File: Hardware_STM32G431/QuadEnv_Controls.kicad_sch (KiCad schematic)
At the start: 14 parts, among them J1 Conn_01x04_Male, J2 Conn_01x05_Male, J3 Conn_01x04_Male, J4 Conn_01x04_Male, J5 Gate_Out, J6 Env_Out

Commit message: First draft of Panel complete
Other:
- company: (none) -> Mountjoy Modular
- title: (none) -> QuadEnv Controls
- moved on the sheet: D1, D2, D3, D4, J4, J5, J6, RV1, RV2, RV3, RV4

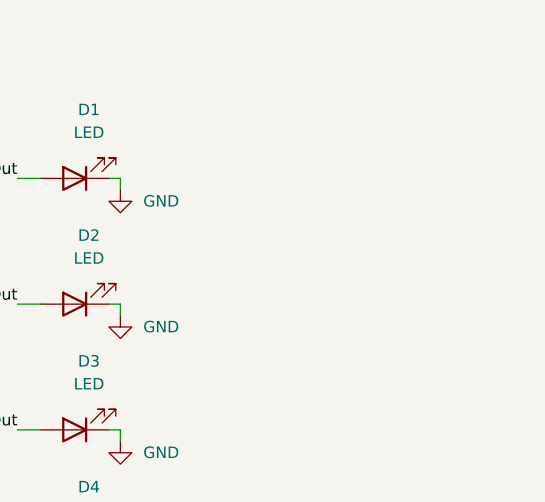
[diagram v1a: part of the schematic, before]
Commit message: Added PWM Test code
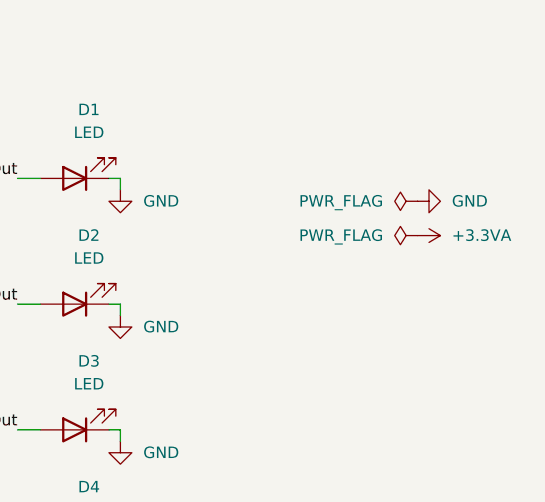
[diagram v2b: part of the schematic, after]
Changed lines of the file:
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@@
     (pin "4")
+  )
+  (symbol (lib_id "power:PWR_FLAG") (at 241.3 46.99 90) (unit 1)
+    (in_bom yes) (on_board yes) (fields_autoplaced)
+    (property "Reference" "#FLG02" (id 0) (at 239.395 46.99 0)
+      (effects (font (size 1.27 1.27)) hide)
+    )
+    (property "Value" "PWR_FLAG" (id 1) (at 237.49 46.9899 90)
+      (effects (font (size 1.27 1.27)) (justify left))
+    )
+    (property "Footprint" "" (id 2) (at 241.3 46.99 0)
+      (effects (font (size 1.27 1.27)) hide)
+    )
+    (property "Datasheet" "~" (id 3) (at 241.3 46.99 0)
+      (effects (font (size 1.27 1.27)) hide)
+    )
+    (pin "1")
   )
   (symbol (lib_id "Device:LED") (at 203.2 40.64 180) (unit 1)
@@
     (pin "2")
   )
+  (symbol (lib_id "power:PWR_FLAG") (at 241.3 43.18 90) (unit 1)
+    (in_bom yes) (on_board yes) (fields_autoplaced)
+    (property "Reference" "#FLG01" (id 0) (at 239.395 43.18 0)
+      (effects (font (size 1.27 1.27)) hide)
+    )
+    (property "Value" "PWR_FLAG" (id 1) (at 237.49 43.1799 90)
+      (effects (font (size 1.27 1.27)) (justify left))
+    )
+    (property "Footprint" "" (id 2) (at 241.3 43.18 0)
+      (effects (font (size 1.27 1.27)) hide)
+    )
+    (property "Datasheet" "~" (id 3) (at 241.3 43.18 0)
+      (effects (font (size 1.27 1.27)) hide)
+    )
+    (pin "1")
+  )
   (symbol (lib_id "Connector:Conn_01x05_Male") (at 59.69 44.45 0) (unit 1)
     (in_bom yes) (on_board yes)
@@
     (pin "4")
   )
+  (symbol (lib_id "power:GND") (at 241.3 43.18 90) (mirror x) (unit 1)
+    (in_bom yes) (on_board yes) (fields_autoplaced)
+    (property "Reference" "#PWR01" (id 0) (at 247.65 43.18 0)
+      (effects (font (size 1.27 1.27)) hide)
+    )
+    (property "Value" "GND" (id 1) (at 245.11 43.1799 90)
+      (effects (font (size 1.27 1.27)) (justify right))
+    )
+    (property "Footprint" "" (id 2) (at 241.3 43.18 0)
+      (effects (font (size 1.27 1.27)) hide)
+    )
+    (property "Datasheet" "" (id 3) (at 241.3 43.18 0)
+      (effects (font (size 1.27 1.27)) hide)
+    )
+    (pin "1")
+  )
   (symbol (lib_id "Device:R_Potentiometer") (at 106.68 49.53 0) (unit 1)
     (in_bom yes) (on_board yes) (fields_autoplaced)
@@
     (pin "2")
     (pin "3")
+  )
+  (symbol (lib_id "power:+3.3VA") (at 241.3 46.99 270) (unit 1)
+    (in_bom yes) (on_board yes) (fields_autoplaced)
+    (property "Reference" "#PWR02" (id 0) (at 237.49 46.99 0)
+      (effects (font (size 1.27 1.27)) hide)
+    )
+    (property "Value" "+3.3VA" (id 1) (at 245.11 46.9899 90)
+      (effects (font (size 1.27 1.27)) (justify left))
+    )
+    (property "Footprint" "" (id 2) (at 241.3 46.99 0)
+      (effects (font (size 1.27 1.27)) hide)
+    )
+    (property "Datasheet" "" (id 3) (at 241.3 46.99 0)
+      (effects (font (size 1.27 1.27)) hide)
+    )
+    (pin "1")
   )
   (symbol (lib_id "Device:LED") (at 203.2 68.58 180) (unit 1)
@@
   )
   (symbol_instances
+    (path "/781d2827-8c57-4c8c-a90e-7fa9a8e3bce3"
+      (reference "#FLG01") (unit 1) (value "PWR_FLAG") (footprint "")
+    )
+    (path "/14afa5e3-66d5-4d5e-b805-932a5af80e37"
+      (reference "#FLG02") (unit 1) (value "PWR_FLAG") (footprint "")
+    )
+    (path "/8b2a71f8-8e19-4c07-809c-0b6873192b65"
+      (reference "#PWR01") (unit 1) (value "GND") (footprint "")
+    )
+    (path "/a579e8f5-f380-4350-a981-d76dba1a11f6"
+      (reference "#PWR02") (unit 1) (value "+3.3VA") (footprint "")
+    )
     (path "/b39f733d-e3d6-4862-b7be-1e5e202f5a4b"
       (reference "#PWR05") (unit 1) (value "+3.3VA") (footprint "")

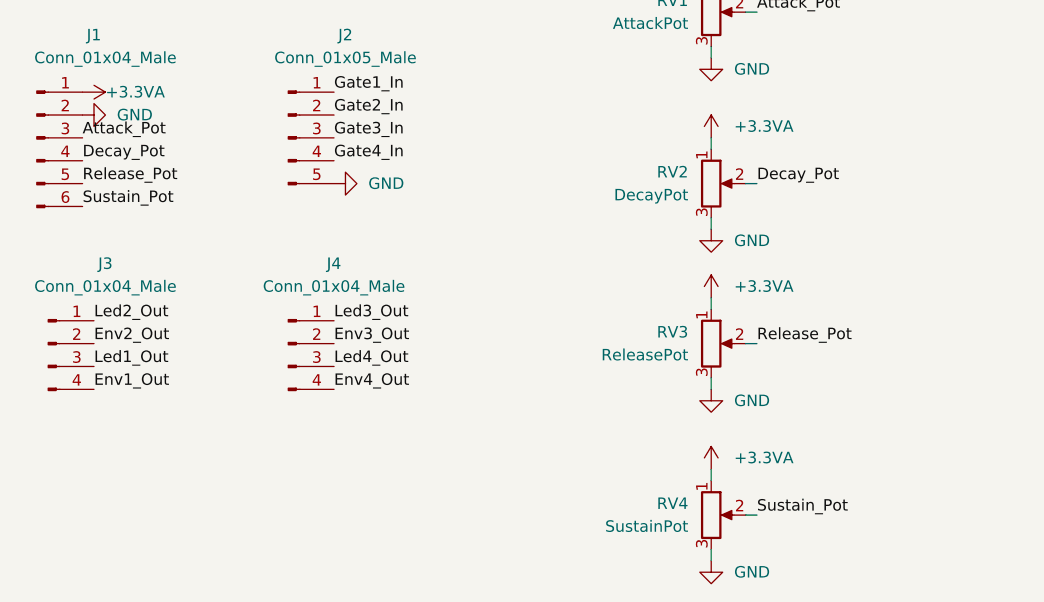
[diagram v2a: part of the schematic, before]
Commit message: Corrections to schematic to fix sustain and release pots being switched
+Updated project to use production module parts and connections
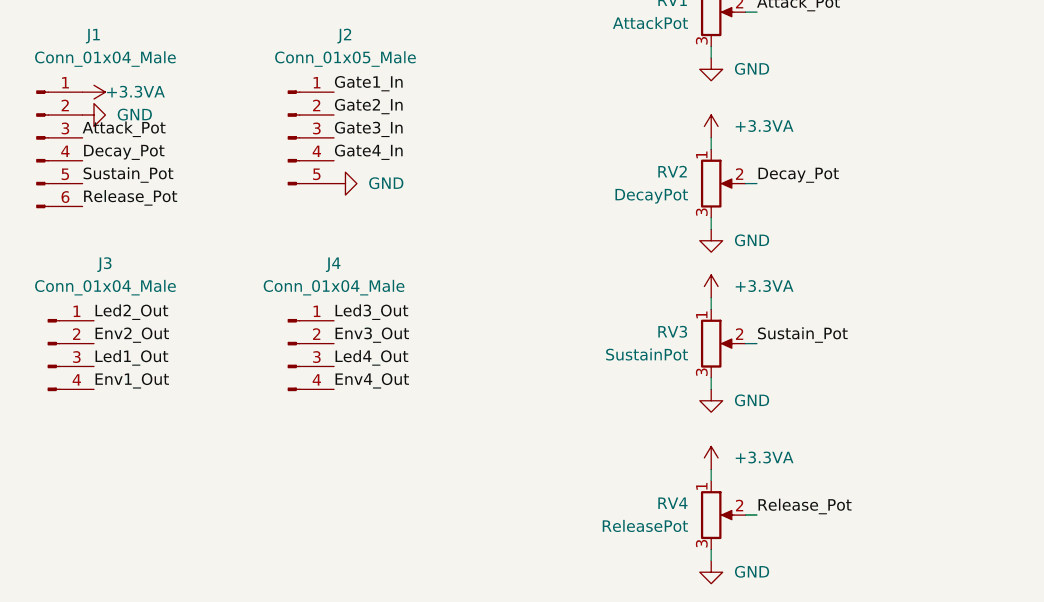
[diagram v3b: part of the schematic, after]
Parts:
- RV3: value ReleasePot -> SustainPot
- RV4: value SustainPot -> ReleasePot
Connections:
- net Release_Pot: now also J1.6 (Pin_6), RV4.2; no longer J1.5 (Pin_5), RV3.2
- net Sustain_Pot: now also J1.5 (Pin_5), RV3.2; no longer J1.6 (Pin_6), RV4.2
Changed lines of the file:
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@@
     (effects (font (size 1.27 1.27)) (justify right bottom))
   )
-  (label "Sustain_Pot" (at 36.83 52.07 0)
+  (label "Sustain_Pot" (at 36.83 49.53 0)
     (effects (font (size 1.27 1.27)) (justify left bottom))
   )
@@
     (effects (font (size 1.27 1.27)) (justify left bottom))
   )
-  (label "Release_Pot" (at 111.76 67.31 0)
+  (label "Release_Pot" (at 111.76 86.36 0)
     (effects (font (size 1.27 1.27)) (justify left bottom))
   )
@@
     (effects (font (size 1.27 1.27)) (justify left bottom))
   )
-  (label "Release_Pot" (at 36.83 49.53 0)
+  (label "Release_Pot" (at 36.83 52.07 0)
     (effects (font (size 1.27 1.27)) (justify left bottom))
   )
@@
     (effects (font (size 1.27 1.27)) (justify left bottom))
   )
-  (label "Sustain_Pot" (at 111.76 86.36 0)
+  (label "Sustain_Pot" (at 111.76 67.31 0)
     (effects (font (size 1.27 1.27)) (justify left bottom))
   )
@@
       (effects (font (size 1.27 1.27)) (justify right))
     )
-    (property "Value" "SustainPot" (id 1) (at 104.14 87.6299 0)
+    (property "Value" "ReleasePot" (id 1) (at 104.14 87.6299 0)
       (effects (font (size 1.27 1.27)) (justify right))
     )
@@
       (effects (font (size 1.27 1.27)) (justify right))
     )
-    (property "Value" "ReleasePot" (id 1) (at 104.14 68.5799 0)
+    (property "Value" "SustainPot" (id 1) (at 104.14 68.5799 0)
       (effects (font (size 1.27 1.27)) (justify right))
     )
@@
     )
     (path "/3fb71fd2-1e6c-4fed-be40-5f5a7bfb3908"
-      (reference "RV3") (unit 1) (value "ReleasePot") (footprint "Custom_Footprints:Alpha_9mm_Potentiometer_Aligned")
+      (reference "RV3") (unit 1) (value "SustainPot") (footprint "Custom_Footprints:Alpha_9mm_Potentiometer_Aligned")
     )
     (path "/191ea6f3-0ad2-4f71-8573-7510f6af6ffa"
-      (reference "RV4") (unit 1) (value "SustainPot") (footprint "Custom_Footprints:Alpha_9mm_Potentiometer_Aligned")
-    )
-  )
+      (reference "RV4") (unit 1) (value "ReleasePot") (footprint "Custom_Footprints:Alpha_9mm_Potentiometer_Aligned")
+    )
+  )

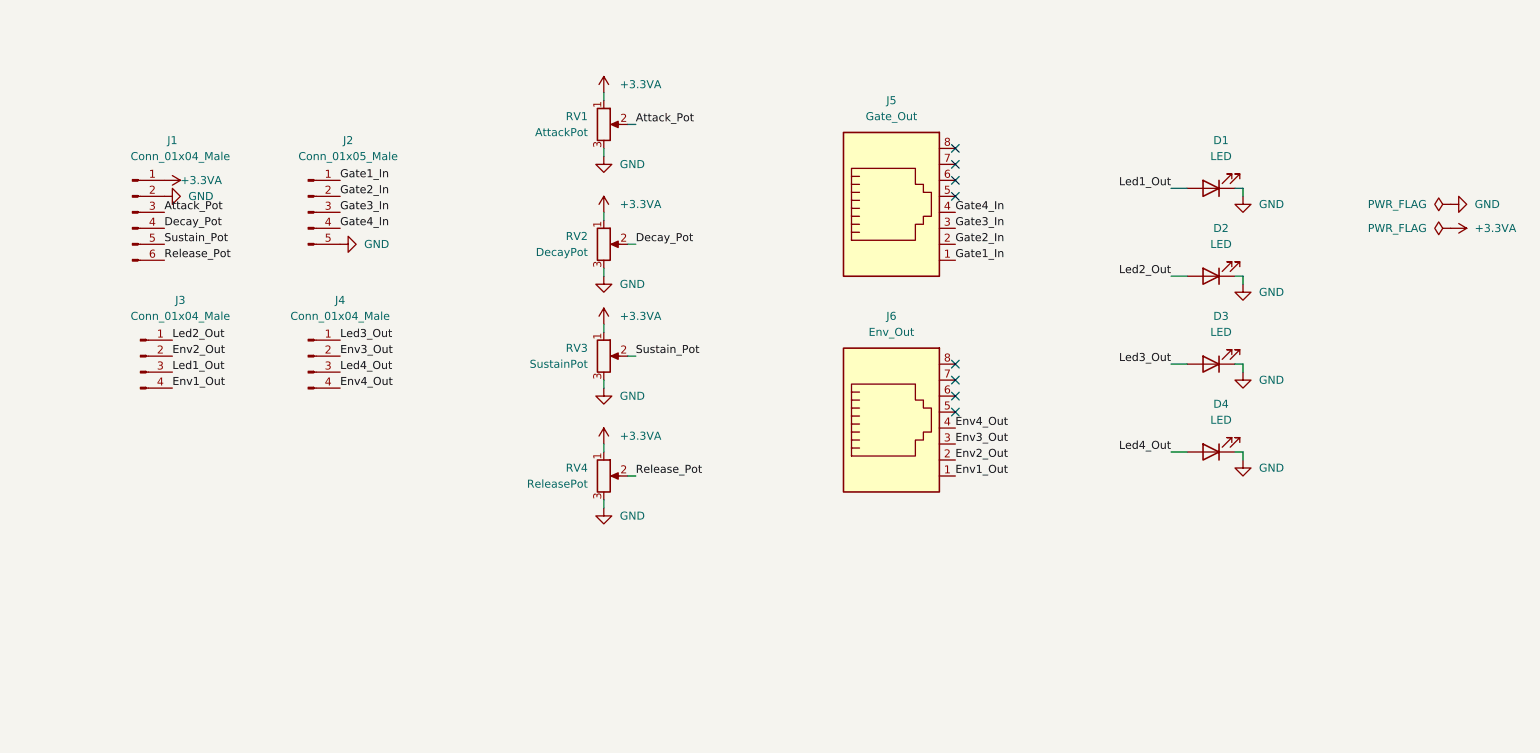
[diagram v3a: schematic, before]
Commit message: Started adding readme;
Clean CubeIDE project created to fix issues in current project
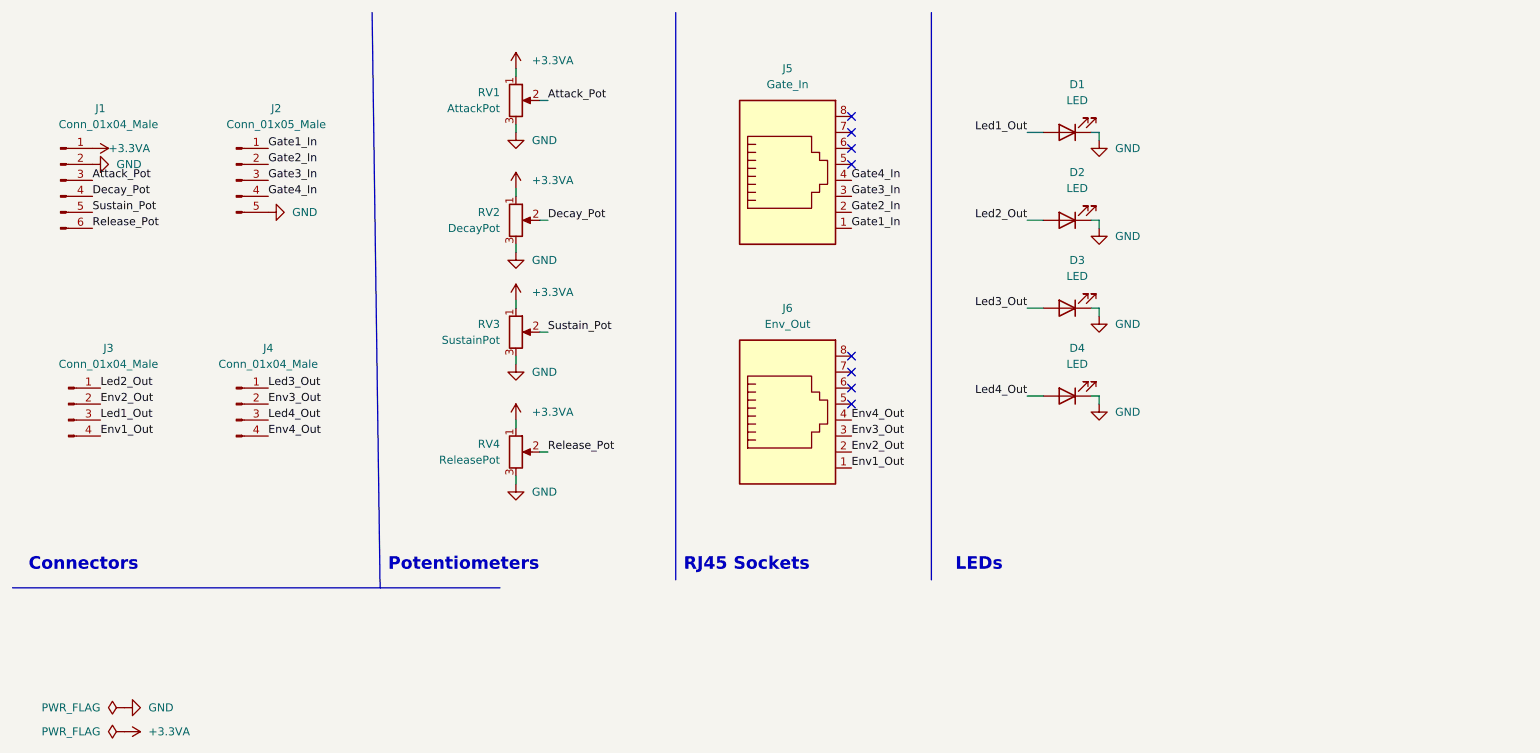
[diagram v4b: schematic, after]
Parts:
- J5: value Gate_Out -> Gate_In
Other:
- note added: "Connectors"
- note added: "LEDs"
- note added: "Potentiometers"
- note added: "RJ45 Sockets"
- moved on the sheet: D1, D2, D3, D4, J1, J2, J3, J4, J5, J6, RV1, RV2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
